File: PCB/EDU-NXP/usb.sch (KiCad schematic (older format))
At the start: 7 parts, among them J2 ZX62-AB-5P8, U2 PRTR5V0U2X

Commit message: BOM actualizado
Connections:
- net CHJ2: now also J2.8 (P8), J2.9 (P9), U2.1 (GND)
- net GND: no longer U2.1 (GND)
- net USB_DM: now also TR1.3; no longer TR1.2
- net USB_DP: now also TR1.2; no longer TR1.3
- net at J2.2 (P2): now also TR1.4; no longer TR1.1
- net at J2.3 (P3): now also TR1.1; no longer TR1.4
- no-connect marks 2 -> 0
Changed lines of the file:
@@
 LIBS:pbss5240xf
 LIBS:LED_RGB
-LIBS:Logo
 LIBS:edu-ciaa-logo
+LIBS:EDUCIAANXP
 LIBS:edu-ciaa-nxp-cache
 EELAYER 27 0
@@
 encoding utf-8
 Sheet 3 7
-Title "EDU CIAA USB OTG"
-Date "23 jul 2014"
+Title "EDU CIAA USB"
+Date "28 aug 2014"
 Rev "1.0"
 Comp ""
@@
 $EndComp
 $Comp
-L GND #PWR010
-U 1 1 52BC3F9D
-P 5150 5000
-F 0 "#PWR010" H 5150 5000 30  0001 C CNN
-F 1 "GND" H 5150 4930 30  0001 C CNN
-F 2 "" H 5150 5000 60  0000 C CNN
-F 3 "" H 5150 5000 60  0000 C CNN
-	1    5150 5000
-	1    0    0    -1
-$EndComp
-Wire Wire Line
-	6450 3300 6450 4550
-Wire Wire Line
-	6450 4550 6250 4550
-Wire Wire Line
-	5350 4750 5250 4750
-Wire Wire Line
-	5250 4750 5250 3450
-Wire Wire Line
-	6250 4750 6350 4750
-Wire Wire Line
-	6350 4750 6350 3600
-Wire Wire Line
-	5150 5000 5150 4550
-Wire Wire Line
-	5150 4550 5350 4550
-$Comp
 L CAPAPOL C3
 U 1 1 52BC4098
@@
 	1    0    0    -1
 $EndComp
-Wire Wire Line
-	7200 4850 7200 4950
-Wire Wire Line
-	7550 4950 7550 4850
-$Comp
-L GND #PWR011
+$Comp
+L GND #PWR010
 U 1 1 52BC411A
 P 7550 4950
-F 0 "#PWR011" H 7550 4950 30  0001 C CNN
+F 0 "#PWR010" H 7550 4950 30  0001 C CNN
 F 1 "GND" H 7550 4880 30  0001 C CNN
 F 2 "" H 7550 4950 60  0000 C CNN
@@
 $EndComp
 $Comp
-L GND #PWR012
+L GND #PWR011
 U 1 1 52BC4129
 P 7200 4950
-F 0 "#PWR012" H 7200 4950 30  0001 C CNN
+F 0 "#PWR011" H 7200 4950 30  0001 C CNN
 F 1 "GND" H 7200 4880 30  0001 C CNN
 F 2 "" H 7200 4950 60  0000 C CNN
@@
 	1    0    0    -1
 $EndComp
-Wire Wire Line
-	7200 3300 7200 4450
-Wire Wire Line
-	7550 3300 7550 4450
-Connection ~ 7200 3300
-Connection ~ 7550 3300
-Connection ~ 6350 3600
-Connection ~ 5250 3450
 $Comp
 L CONN_9 J2
@@
 	1    0    0    -1
 $EndComp
-Wire Wire Line
-	10150 3400 9400 3400
-Wire Wire Line
-	9400 3400 9400 3450
-Wire Wire Line
-	10150 3500 9500 3500
-Wire Wire Line
-	9500 3500 9500 3600
-Wire Wire Line
-	10150 3600 9600 3600
-Wire Wire Line
-	9600 3600 9600 3750
-Wire Wire Line
-	9600 3750 1600 3750
-Wire Wire Line
-	10150 3700 9700 3700
-Wire Wire Line
-	9700 3700 9700 4950
-$Comp
-L GND #PWR013
+$Comp
+L GND #PWR012
 U 1 1 52BC45E9
 P 9700 4950
-F 0 "#PWR013" H 9700 4950 30  0001 C CNN
+F 0 "#PWR012" H 9700 4950 30  0001 C CNN
 F 1 "GND" H 9700 4880 30  0001 C CNN
 F 2 "" H 9700 4950 60  0000 C CNN
@@
 	1    0    0    -1
 $EndComp
-Connection ~ 10050 4100
-Wire Wire Line
-	10050 3800 10150 3800
-Connection ~ 10050 4000
-Wire Wire Line
-	10150 3900 10050 3900
-Connection ~ 10050 3900
-Connection ~ 6450 3300
-Wire Wire Line
-	10050 3800 10050 4150
-Wire Wire Line
-	10050 4850 10050 4900
-Wire Wire Line
-	10050 4900 9700 4900
-Connection ~ 9700 4900
 $Comp
 L FILTER FB2
@@
 	-1   0    0    1
 $EndComp
-Wire Wire Line
-	8550 3300 10150 3300
-Wire Wire Line
-	1600 3300 7850 3300
 $Comp
 L TRASF_UNIP TR1
 U 1 1 52DDB29E
 P 8200 4100
-F 0 "TR1" V 8600 4100 60  0000 C CNN
-F 1 "DLW21HN900SQ2" V 8500 4100 60  0000 C CNN
+F 0 "TR1" V 8450 4100 60  0000 C CNN
+F 1 "DLW21HN900SQ2" V 7900 4100 60  0000 C CNN
 F 2 "" H 8200 4100 60  0000 C CNN
 F 3 "" H 8200 4100 60  0000 C CNN
 	1    8200 4100
-	0    1    1    0
-$EndComp
-Wire Wire Line
-	9400 3450 8350 3450
-Wire Wire Line
-	8350 3450 8350 3900
-Wire Wire Line
-	8450 4300 8450 3600
-Wire Wire Line
-	8450 3600 9500 3600
-Wire Wire Line
-	8450 4300 8350 4300
-Wire Wire Line
-	8050 3450 8050 3900
-Wire Wire Line
-	1600 3450 8050 3450
-Wire Wire Line
-	1600 3600 7950 3600
-Wire Wire Line
-	7950 3600 7950 4300
-Wire Wire Line
-	7950 4300 8050 4300
-NoConn ~ 10150 4000
-NoConn ~ 10150 4100
+	0    1    -1   0
+$EndComp
 $Comp
 L LOGO #G3
@@
 	1    0    0    -1
 $EndComp
-Wire Wire Line
-	10050 4000 9800 4000
-Text Label 9800 4000 0    60   ~ 0
+Text Label 4850 4550 0    60   ~ 0
 CHJ2
+Text Label 9800 3900 0    60   ~ 0
+CHJ2
+$Comp
+L PWR_FLAG #FLG013
+U 1 1 5401E321
+P 4800 4350
+F 0 "#FLG013" H 4800 4445 30  0001 C CNN
+F 1 "PWR_FLAG" H 4800 4530 30  0000 C CNN
+F 2 "" H 4800 4350 60  0000 C CNN
+F 3 "" H 4800 4350 60  0000 C CNN
+	1    4800 4350
+	1    0    0    -1
+$EndComp
+Wire Wire Line
+	6450 3300 6450 4550
+Wire Wire Line
+	6450 4550 6250 4550
+Wire Wire Line
+	5350 4750 5250 4750
+Wire Wire Line
+	5250 4750 5250 3450
+Wire Wire Line
+	6250 4750 6350 4750
+Wire Wire Line
+	6350 4750 6350 3600
+Wire Wire Line
+	4800 4550 5350 4550
+Wire Wire Line
+	7200 4850 7200 4950
+Wire Wire Line
+	7550 4950 7550 4850
+Wire Wire Line
+	7200 3300 7200 4450
+Wire Wire Line
+	7550 3300 7550 4450
+Connection ~ 7200 3300
+Connection ~ 7550 3300
+Connection ~ 6350 3600
+Connection ~ 5250 3450
+Wire Wire Line
+	10150 3400 9400 3400
+Wire Wire Line
+	9400 3400 9400 3450
+Wire Wire Line
+	10150 3500 9500 3500
+Wire Wire Line
+	9500 3500 9500 3600
+Wire Wire Line
+	10150 3600 9600 3600
+Wire Wire Line
+	9600 3600 9600 3750
+Wire Wire Line
+	9600 3750 1600 3750
+Wire Wire Line
+	10150 3700 9700 3700
+Wire Wire Line
+	9700 3700 9700 4950
+Connection ~ 10050 4100
+Wire Wire Line
+	10050 3800 10150 3800
+Connection ~ 10050 4000
+Wire Wire Line
+	9800 3900 10150 3900
+Connection ~ 10050 3900
+Connection ~ 6450 3300
+Wire Wire Line
+	10050 3800 10050 4150
+Wire Wire Line
+	10050 4850 10050 4900
+Wire Wire Line
+	10050 4900 9700 4900
+Connection ~ 9700 4900
+Wire Wire Line
+	8550 3300 10150 3300
+Wire Wire Line
+	1600 3300 7850 3300
+Wire Wire Line
+	9400 3450 8350 3450
+Wire Wire Line
+	8350 3450 8350 3900
+Wire Wire Line
+	9500 3600 8450 3600
+Wire Wire Line
+	8050 3450 8050 3900
+Wire Wire Line
+	1600 3450 8050 3450
+Wire Wire Line
+	1600 3600 7950 3600
+Wire Wire Line
+	7950 3600 7950 4300
+Wire Wire Line
+	7950 4300 8050 4300
+Wire Wire Line
+	10150 4000 10050 4000
+Wire Wire Line
+	10150 4100 10050 4100
+Wire Wire Line
+	4800 4350 4800 4550
+Wire Wire Line
+	8450 4300 8350 4300
+Wire Wire Line
+	8450 3600 8450 4300
 $EndSCHEMATC

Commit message: Se agregó USB-OTH en los esquemáticos
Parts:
- added C50: 100nF, ~, symbol C
- added R16, R17: 10k, ~, symbol R
- added U9: MIC2025, ~, symbol MIC2025
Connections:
- net labels added: +3.3V, +5V, USB_PPWR, USB_PWR_FAULT
- wire segments 40 -> 58
- no-connect marks 0 -> 2
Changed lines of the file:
@@
 EESchema Schematic File Version 2
-LIBS:power
-LIBS:device
-LIBS:transistors
-LIBS:conn
-LIBS:linear
-LIBS:regul
-LIBS:74xx
-LIBS:cmos4000
-LIBS:adc-dac
-LIBS:memory
-LIBS:xilinx
-LIBS:special
-LIBS:microcontrollers
-LIBS:dsp
-LIBS:microchip
-LIBS:analog_switches
-LIBS:motorola
-LIBS:texas
-LIBS:intel
-LIBS:audio
-LIBS:interface
-LIBS:digital-audio
-LIBS:philips
-LIBS:display
-LIBS:cypress
-LIBS:siliconi
-LIBS:opto
-LIBS:atmel
-LIBS:contrib
-LIBS:valves
-LIBS:74LVC1G04GW
-LIBS:amesser-ad
-LIBS:amesser-cmos4000
-LIBS:amesser-conn
-LIBS:amesser-discrete
-LIBS:amesser-linear
-LIBS:amesser-power
-LIBS:amesser-usb
-LIBS:audio-vlsi
-LIBS:bat54_c
-LIBS:BLM15HG6015N1D
-LIBS:g5v2
-LIBS:lm2596
-LIBS:mcu-nxp
-LIBS:mcu-st
-LIBS:MIC2025
-LIBS:net-phy
-LIBS:nsi50010yt1g
-LIBS:PRTR5V0U2X
-LIBS:regulators
-LIBS:rs485_rs232_can
-LIBS:s25fl032p0xmfi013
-LIBS:SCHA5B0200
-LIBS:Si50x
-LIBS:Transil_diode
-LIBS:w_device
-LIBS:LPC4337JBD144
-LIBS:IS42S16400F
-LIBS:TXB0108
-LIBS:FT2232H
-LIBS:93CXX
-LIBS:TJA1040
-LIBS:tvs
-LIBS:PBSS5240
-LIBS:pbss5240xf
-LIBS:LED_RGB
-LIBS:edu-ciaa-logo
-LIBS:EDUCIAANXP
+LIBS:edu-ciaa-nxp
 LIBS:edu-ciaa-nxp-cache
 EELAYER 27 0
@@
 Sheet 3 7
 Title "EDU CIAA USB"
-Date "28 aug 2014"
+Date "25 sep 2014"
 Rev "1.0"
 Comp ""
@@
 Wire Wire Line
 	8450 3600 8450 4300
+Text HLabel 1600 4200 0    60   Input ~ 0
+USB_PPWR
+Text HLabel 1600 4350 0    60   Input ~ 0
+USB_PWR_FAULT
+$Comp
+L MIC2025 U9
+U 1 1 542313E7
+P 3150 5300
+F 0 "U9" H 3100 5900 60  0000 L CNN
+F 1 "MIC2025" H 2950 4650 60  0000 L CNN
+F 2 "~" H 3150 5300 60  0000 C CNN
+F 3 "~" H 3150 5300 60  0000 C CNN
+	1    3150 5300
+	1    0    0    -1
+$EndComp
+Wire Wire Line
+	3900 5400 4400 5400
+Wire Wire Line
+	4400 5400 4400 3300
+Connection ~ 4400 3300
+Wire Wire Line
+	3900 5000 4400 5000
+Connection ~ 4400 5000
+NoConn ~ 3900 5600
+NoConn ~ 2400 5600
+$Comp
+L GND #PWR014
+U 1 1 5423145B
+P 4600 6050
+F 0 "#PWR014" H 4600 6050 30  0001 C CNN
+F 1 "GND" H 4600 5980 30  0001 C CNN
+F 2 "" H 4600 6050 60  0000 C CNN
+F 3 "" H 4600 6050 60  0000 C CNN
+	1    4600 6050
+	1    0    0    -1
+$EndComp
+Wire Wire Line
+	4600 5700 4600 6050
+$Comp
+L GND #PWR015
+U 1 1 54231462
+P 1950 6050
+F 0 "#PWR015" H 1950 6050 30  0001 C CNN
+F 1 "GND" H 1950 5980 30  0001 C CNN
+F 2 "" H 1950 6050 60  0000 C CNN
+F 3 "" H 1950 6050 60  0000 C CNN
+	1    1950 6050
+	1    0    0    -1
+$EndComp
+Wire Wire Line
+	1950 5400 1950 6050
+Wire Wire Line
+	2400 5400 1950 5400
+$Comp
+L C C50
+U 1 1 542314A2
+P 4600 5500
+F 0 "C50" H 4600 5600 40  0000 L CNN
+F 1 "100nF" H 4606 5415 40  0000 L CNN
+F 2 "~" H 4638 5350 30  0000 C CNN
+F 3 "~" H 4600 5500 60  0000 C CNN
+	1    4600 5500
+	1    0    0    -1
+$EndComp
+Wire Wire Line
+	3900 5200 4600 5200
+Wire Wire Line
+	4600 5100 4600 5300
+Connection ~ 4600 5200
+$Comp
+L +5V #PWR016
+U 1 1 542315D6
+P 4600 5100
+F 0 "#PWR016" H 4600 5190 20  0001 C CNN
+F 1 "+5V" H 4600 5190 30  0000 C CNN
+F 2 "" H 4600 5100 60  0000 C CNN
+F 3 "" H 4600 5100 60  0000 C CNN
+	1    4600 5100
+	1    0    0    -1
+$EndComp
+$Comp
+L +3.3V #PWR017
+U 1 1 542315E1
+P 1300 4600
+F 0 "#PWR017" H 1300 4560 30  0001 C CNN
+F 1 "+3.3V" H 1300 4710 30  0000 C CNN
+F 2 "" H 1300 4600 60  0000 C CNN
+F 3 "" H 1300 4600 60  0000 C CNN
+	1    1300 4600
+	1    0    0    -1
+$EndComp
+$Comp
+L R R16
+U 1 1 542315EC
+P 1300 4900
+F 0 "R16" V 1380 4900 40  0000 C CNN
+F 1 "10k" V 1307 4901 40  0000 C CNN
+F 2 "~" V 1230 4900 30  0000 C CNN
+F 3 "~" H 1300 4900 30  0000 C CNN
+	1    1300 4900
+	-1   0    0    1
+$EndComp
+$Comp
+L R R17
+U 1 1 542315F2
+P 2000 4500
+F 0 "R17" V 2080 4500 40  0000 C CNN
+F 1 "10k" V 2007 4501 40  0000 C CNN
+F 2 "~" V 1930 4500 30  0000 C CNN
+F 3 "~" H 2000 4500 30  0000 C CNN
+	1    2000 4500
+	-1   0    0    1
+$EndComp
+Wire Wire Line
+	2400 5000 2300 5000
+Wire Wire Line
+	2300 5000 2300 4200
+Wire Wire Line
+	2300 4200 1600 4200
+Wire Wire Line
+	1600 4350 1700 4350
+Wire Wire Line
+	1700 4350 1700 5200
+Wire Wire Line
+	1300 5200 2400 5200
+Wire Wire Line
+	1300 4600 1300 4650
+Wire Wire Line
+	1300 5150 1300 5200
+Connection ~ 1700 5200
+Wire Wire Line
+	2000 4250 2000 4200
+Connection ~ 2000 4200
+$Comp
+L GND #PWR018
+U 1 1 542317A0
+P 2000 4800
+F 0 "#PWR018" H 2000 4800 30  0001 C CNN
+F 1 "GND" H 2000 4730 30  0001 C CNN
+F 2 "" H 2000 4800 60  0000 C CNN
+F 3 "" H 2000 4800 60  0000 C CNN
+	1    2000 4800
+	1    0    0    -1
+$EndComp
+Wire Wire Line
+	2000 4750 2000 4800
 $EndSCHEMATC

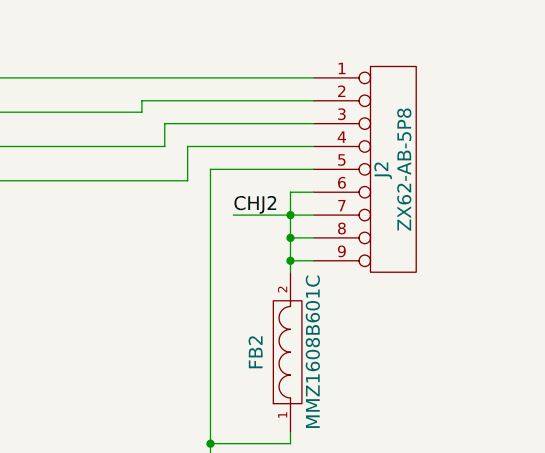
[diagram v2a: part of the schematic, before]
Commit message: Modificaciones del PCB propuestos por la segunda revisión
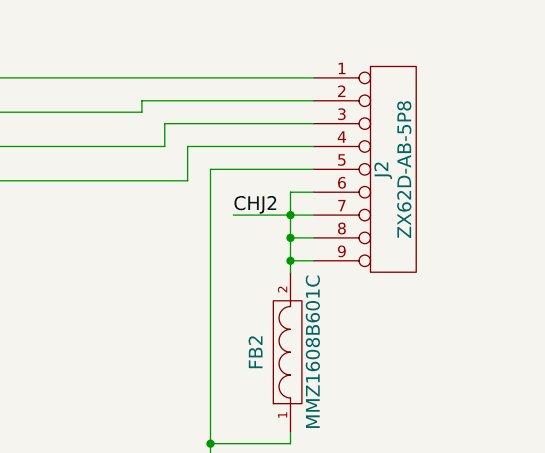
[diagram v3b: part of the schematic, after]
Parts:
- J2: value ZX62-AB-5P8 -> ZX62D-AB-5P8
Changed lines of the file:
@@
 Sheet 3 7
 Title "EDU CIAA USB"
-Date "25 sep 2014"
+Date "22 oct 2014"
 Rev "1.0"
 Comp ""
@@
 $EndComp
 $Comp
-L GND #PWR010
+L GND #PWR16
 U 1 1 52BC411A
 P 7550 4950
-F 0 "#PWR010" H 7550 4950 30  0001 C CNN
+F 0 "#PWR16" H 7550 4950 30  0001 C CNN
 F 1 "GND" H 7550 4880 30  0001 C CNN
 F 2 "" H 7550 4950 60  0000 C CNN
@@
 $EndComp
 $Comp
-L GND #PWR011
+L GND #PWR15
 U 1 1 52BC4129
 P 7200 4950
-F 0 "#PWR011" H 7200 4950 30  0001 C CNN
+F 0 "#PWR15" H 7200 4950 30  0001 C CNN
 F 1 "GND" H 7200 4880 30  0001 C CNN
 F 2 "" H 7200 4950 60  0000 C CNN
@@
 P 10500 3700
 F 0 "J2" V 10450 3700 60  0000 C CNN
-F 1 "ZX62-AB-5P8" V 10550 3700 60  0000 C CNN
+F 1 "ZX62D-AB-5P8" V 10550 3700 60  0000 C CNN
 F 2 "" H 10500 3700 60  0000 C CNN
 F 3 "" H 10500 3700 60  0000 C CNN
@@
 $EndComp
 $Comp
-L GND #PWR012
+L GND #PWR17
 U 1 1 52BC45E9
 P 9700 4950
-F 0 "#PWR012" H 9700 4950 30  0001 C CNN
+F 0 "#PWR17" H 9700 4950 30  0001 C CNN
 F 1 "GND" H 9700 4880 30  0001 C CNN
 F 2 "" H 9700 4950 60  0000 C CNN
@@
 CHJ2
 $Comp
-L PWR_FLAG #FLG013
+L PWR_FLAG #FLG1
 U 1 1 5401E321
 P 4800 4350
-F 0 "#FLG013" H 4800 4445 30  0001 C CNN
+F 0 "#FLG1" H 4800 4445 30  0001 C CNN
 F 1 "PWR_FLAG" H 4800 4530 30  0000 C CNN
 F 2 "" H 4800 4350 60  0000 C CNN
@@
 NoConn ~ 2400 5600
 $Comp
-L GND #PWR014
+L GND #PWR14
 U 1 1 5423145B
 P 4600 6050
-F 0 "#PWR014" H 4600 6050 30  0001 C CNN
+F 0 "#PWR14" H 4600 6050 30  0001 C CNN
 F 1 "GND" H 4600 5980 30  0001 C CNN
 F 2 "" H 4600 6050 60  0000 C CNN
@@
 	4600 5700 4600 6050
 $Comp
-L GND #PWR015
+L GND #PWR11
 U 1 1 54231462
 P 1950 6050
-F 0 "#PWR015" H 1950 6050 30  0001 C CNN
+F 0 "#PWR11" H 1950 6050 30  0001 C CNN
 F 1 "GND" H 1950 5980 30  0001 C CNN
 F 2 "" H 1950 6050 60  0000 C CNN
@@
 Connection ~ 4600 5200
 $Comp
-L +5V #PWR016
+L +5V #PWR13
 U 1 1 542315D6
 P 4600 5100
-F 0 "#PWR016" H 4600 5190 20  0001 C CNN
+F 0 "#PWR13" H 4600 5190 20  0001 C CNN
 F 1 "+5V" H 4600 5190 30  0000 C CNN
 F 2 "" H 4600 5100 60  0000 C CNN
@@
 $EndComp
 $Comp
-L +3.3V #PWR017
+L +3.3V #PWR10
 U 1 1 542315E1
 P 1300 4600
-F 0 "#PWR017" H 1300 4560 30  0001 C CNN
+F 0 "#PWR10" H 1300 4560 30  0001 C CNN
 F 1 "+3.3V" H 1300 4710 30  0000 C CNN
 F 2 "" H 1300 4600 60  0000 C CNN
@@
 Connection ~ 2000 4200
 $Comp
-L GND #PWR018
+L GND #PWR12
 U 1 1 542317A0
 P 2000 4800
-F 0 "#PWR018" H 2000 4800 30  0001 C CNN
+F 0 "#PWR12" H 2000 4800 30  0001 C CNN
 F 1 "GND" H 2000 4730 30  0001 C CNN
 F 2 "" H 2000 4800 60  0000 C CNN

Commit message: Logo Open Hardware
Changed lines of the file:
@@
 Sheet 3 7
 Title "EDU CIAA USB"
-Date "22 oct 2014"
+Date "26 oct 2014"
 Rev "1.0"
 Comp ""
@@
 $EndComp
 $Comp
-L GND #PWR16
+L GND #PWR010
 U 1 1 52BC411A
 P 7550 4950
-F 0 "#PWR16" H 7550 4950 30  0001 C CNN
+F 0 "#PWR010" H 7550 4950 30  0001 C CNN
 F 1 "GND" H 7550 4880 30  0001 C CNN
 F 2 "" H 7550 4950 60  0000 C CNN
@@
 $EndComp
 $Comp
-L GND #PWR15
+L GND #PWR011
 U 1 1 52BC4129
 P 7200 4950
-F 0 "#PWR15" H 7200 4950 30  0001 C CNN
+F 0 "#PWR011" H 7200 4950 30  0001 C CNN
 F 1 "GND" H 7200 4880 30  0001 C CNN
 F 2 "" H 7200 4950 60  0000 C CNN
@@
 $EndComp
 $Comp
-L GND #PWR17
+L GND #PWR012
 U 1 1 52BC45E9
 P 9700 4950
-F 0 "#PWR17" H 9700 4950 30  0001 C CNN
+F 0 "#PWR012" H 9700 4950 30  0001 C CNN
 F 1 "GND" H 9700 4880 30  0001 C CNN
 F 2 "" H 9700 4950 60  0000 C CNN
@@
 $EndComp
 $Comp
-L LOGO #G3
+L LOGO #G6
 U 1 1 53C3FC54
 P 10650 6600
-F 0 "#G3" H 10650 6197 60  0001 C CNN
+F 0 "#G6" H 10650 6197 60  0001 C CNN
 F 1 "LOGO" H 10650 7003 60  0001 C CNN
 F 2 "" H 10650 6600 60  0000 C CNN
@@
 CHJ2
 $Comp
-L PWR_FLAG #FLG1
+L PWR_FLAG #FLG013
 U 1 1 5401E321
 P 4800 4350
-F 0 "#FLG1" H 4800 4445 30  0001 C CNN
+F 0 "#FLG013" H 4800 4445 30  0001 C CNN
 F 1 "PWR_FLAG" H 4800 4530 30  0000 C CNN
 F 2 "" H 4800 4350 60  0000 C CNN
@@
 NoConn ~ 2400 5600
 $Comp
-L GND #PWR14
+L GND #PWR014
 U 1 1 5423145B
 P 4600 6050
-F 0 "#PWR14" H 4600 6050 30  0001 C CNN
+F 0 "#PWR014" H 4600 6050 30  0001 C CNN
 F 1 "GND" H 4600 5980 30  0001 C CNN
 F 2 "" H 4600 6050 60  0000 C CNN
@@
 	4600 5700 4600 6050
 $Comp
-L GND #PWR11
+L GND #PWR015
 U 1 1 54231462
 P 1950 6050
-F 0 "#PWR11" H 1950 6050 30  0001 C CNN
+F 0 "#PWR015" H 1950 6050 30  0001 C CNN
 F 1 "GND" H 1950 5980 30  0001 C CNN
 F 2 "" H 1950 6050 60  0000 C CNN
@@
 Connection ~ 4600 5200
 $Comp
-L +5V #PWR13
+L +5V #PWR016
 U 1 1 542315D6
 P 4600 5100
-F 0 "#PWR13" H 4600 5190 20  0001 C CNN
+F 0 "#PWR016" H 4600 5190 20  0001 C CNN
 F 1 "+5V" H 4600 5190 30  0000 C CNN
 F 2 "" H 4600 5100 60  0000 C CNN
@@
 $EndComp
 $Comp
-L +3.3V #PWR10
+L +3.3V #PWR017
 U 1 1 542315E1
 P 1300 4600
-F 0 "#PWR10" H 1300 4560 30  0001 C CNN
+F 0 "#PWR017" H 1300 4560 30  0001 C CNN
 F 1 "+3.3V" H 1300 4710 30  0000 C CNN
 F 2 "" H 1300 4600 60  0000 C CNN
@@
 Connection ~ 2000 4200
 $Comp
-L GND #PWR12
+L GND #PWR018
 U 1 1 542317A0
 P 2000 4800
-F 0 "#PWR12" H 2000 4800 30  0001 C CNN
+F 0 "#PWR018" H 2000 4800 30  0001 C CNN
 F 1 "GND" H 2000 4730 30  0001 C CNN
 F 2 "" H 2000 4800 60  0000 C CNN
@@
 Wire Wire Line
 	2000 4750 2000 4800
+$Comp
+L OSHWA #G5
+U 1 1 544CF18B
+P 9700 6700
+F 0 "#G5" H 9670 7100 60  0001 C CNN
+F 1 "OSHWA" H 9700 7003 60  0001 C CNN
+F 2 "~" H 9700 6700 60  0000 C CNN
+F 3 "~" H 9700 6700 60  0000 C CNN
+	1    9700 6700
+	1    0    0    -1
+$EndComp
 $EndSCHEMATC
